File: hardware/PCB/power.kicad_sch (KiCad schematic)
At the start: 34 parts, among them J1 Screw_Terminal_01x02, U1 TPS62933, U2 TPS56837Hx, U4 TPS56837Hx

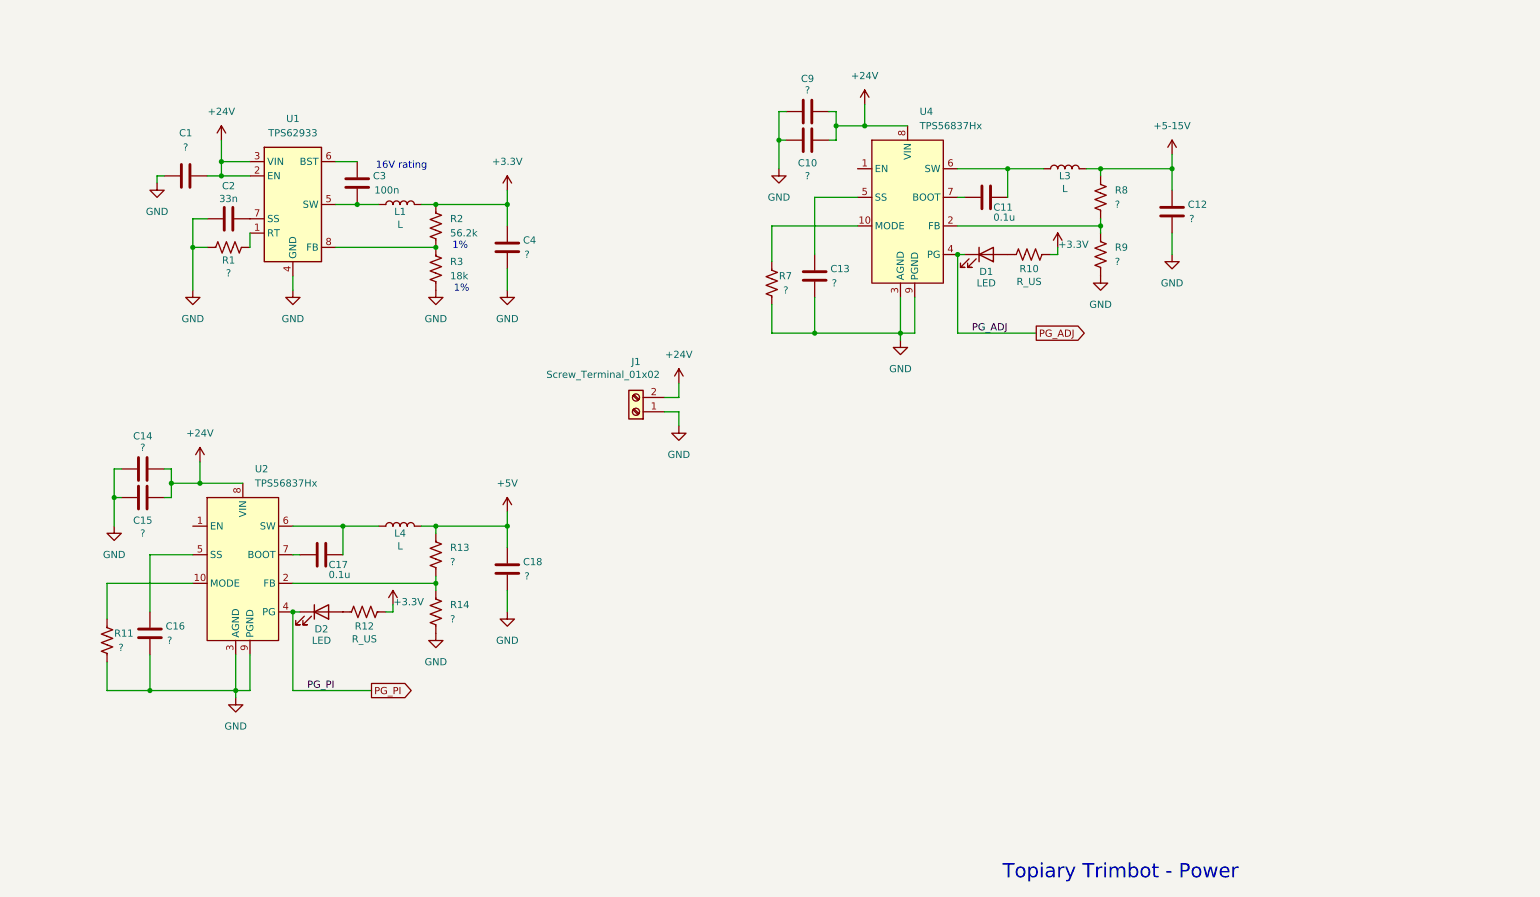
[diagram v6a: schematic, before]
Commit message: Schematic - Power Components
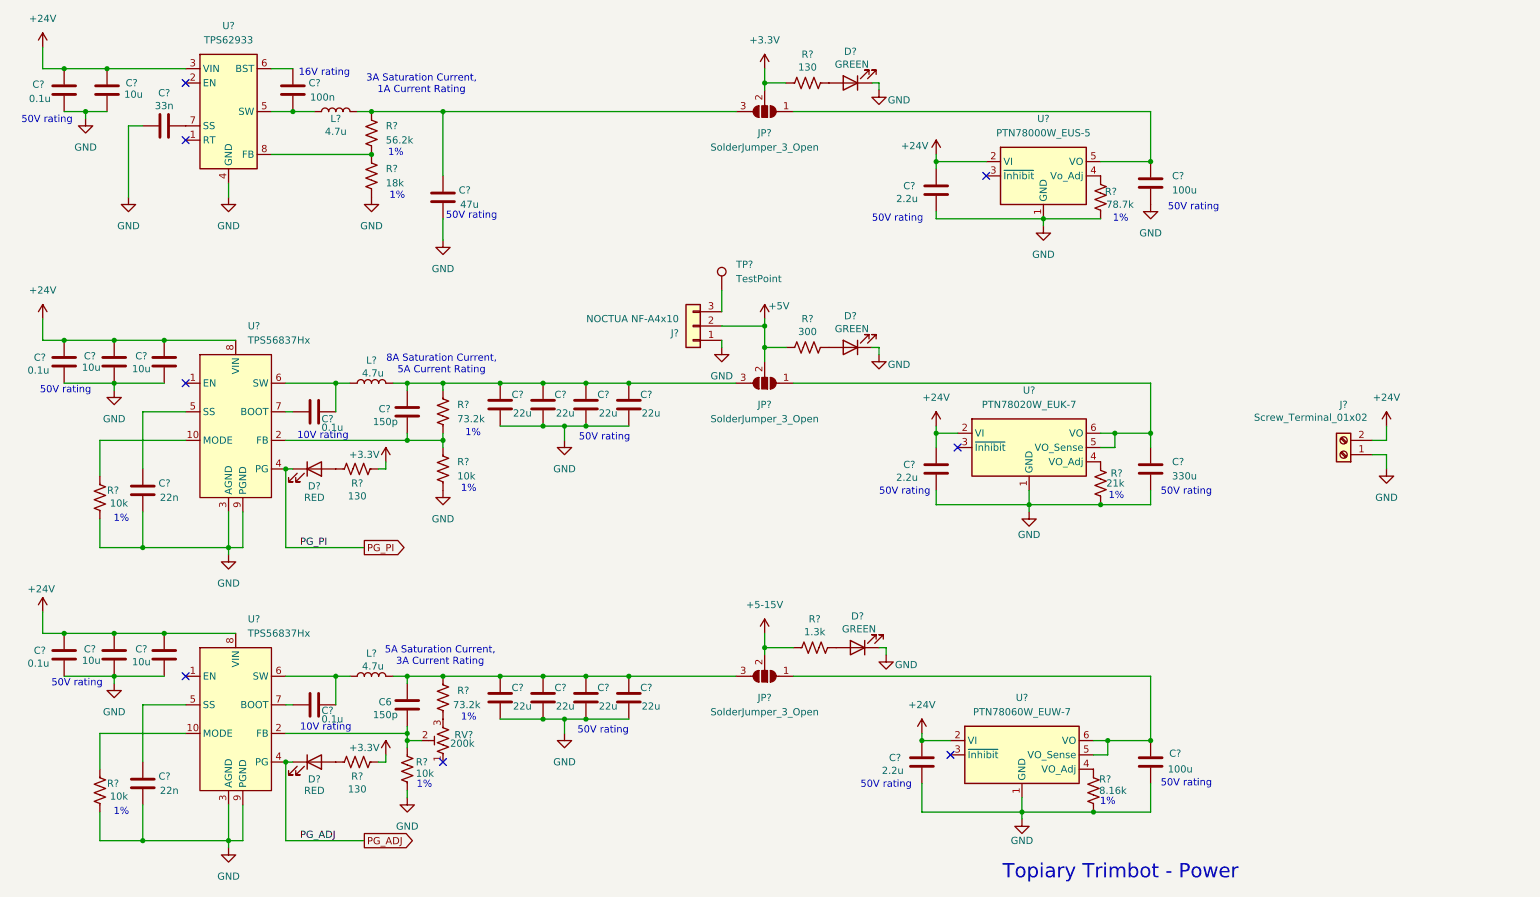
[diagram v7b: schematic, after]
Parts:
- removed C10, C12, C13, C9: ?, symbol Device:C
- removed C11: 0.1u, symbol Device:C
- removed D1: LED, symbol Device:LED
- removed L3: L, symbol Device:L
- removed R1, R7, R8, R9: ?, symbol Device:R_US
- removed R10: R_US, symbol Device:R_US
- removed U4: TPS56837Hx, CustomFootprints:RPA0010A-MFG, symbol CustomSymbols:TPS56837Hx
- added C6, C?: 150p, symbol Device:C
- added C? (x3): 10u, symbol Device:C
- added C?: 22n, symbol Device:C
- added C? (x7): 22u, symbol Device:C
- added C? (x3): 0.1u, symbol Device:C
- added C? (x3): 2.2u, symbol Device:C
- added C? (x2): 100u, symbol Device:C
- added C?: 330u, symbol Device:C
- added D? (x3): GREEN, symbol Device:LED
- added D?: RED, symbol Device:LED
- added J?: NOCTUA NF-A4x10, symbol Connector_Generic:Conn_01x03
- added JP? (x3): SolderJumper_3_Open, symbol Jumper:SolderJumper_3_Open
- added L?: 4.7u, symbol Device:L
- added R?: 300, symbol Device:R_US
- added R? (x2): 10k, symbol Device:R_US
- added R?: 1.3k, symbol Device:R_US
- added R? (x2): 130, symbol Device:R_US
- added R?: 21k, symbol Device:R_US
- added R?: 8.16k, symbol Device:R_US
- added R?: 73.2k, symbol Device:R_US
- added R?: 78.7k, symbol Device:R_US
- added RV?: 200k, symbol Device:R_Potentiometer_Trim_US
- added TP?: TestPoint, symbol Connector:TestPoint
- added U?: PTN78020W_EUK-7, Module:Texas_EUK_R-PDSS-T7_THT, symbol Converter_DCDC:PTN78020W_EUK-7
- added U?: PTN78000W_EUS-5, Module:Texas_EUS_R-PDSS-T5_THT, symbol Converter_DCDC:PTN78000W_EUS-5
- added U?: PTN78060W_EUW-7, Module:Texas_EUW_R-PDSS-T7_THT, symbol Converter_DCDC:PTN78060W_EUW-7
- added U?: TPS56837Hx, CustomFootprints:RPA0010A-MFG, symbol CustomSymbols:TPS56837Hx
- C?: renamed from C16; value ? -> 22n
- C?: renamed from C1; value ? -> 10u
- C?: renamed from C14; value ? -> 10u
- C?: renamed from C18; value ? -> 22u
- C?: renamed from C4; value ? -> 47u
- C?: renamed from C15; value ? -> 0.1u
- D?: renamed from D2; value LED -> RED
- L?: renamed from L1; value L -> 4.7u
- L?: renamed from L4; value L -> 4.7u
- R?: renamed from R12; value R_US -> 130
- R?: renamed from R11; value ? -> 10k
- R?: renamed from R14; value ? -> 10k
- R?: renamed from R13; value ? -> 73.2k
- renumbered C2 to C?, C17 to C?, C3 to C?, J1 to J?, R3 to R?, R2 to R?, U1 to U?, U2 to U?
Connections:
- net +24V: now also C?.1, C?.1, C?.1, C?.2, C?.2, C?.2, C?.2, C?.2, U?.2 (VI), U?.2 (VI), U?.2 (VI), U?.8 (VIN); no longer U?.2 (EN)
- net +3.3V: now also JP?.2 (C), R?.1, R?.2; no longer C?.1, L?.2, R?.1
- net +5-15V: now also JP?.2 (C), R?.2
- net +5V: now also J?.2 (Pin_2), JP?.2 (C), R?.2; no longer C?.1, L?.2, R?.1
- net GND: now also C?.1, C?.1, C?.1, C?.1, C?.1, C?.2, C?.2, C?.2, C?.2, C?.2, C?.2, C?.2, C?.2, C?.2, C?.2, C?.2, C?.2, C?.2, C?.2, D?.1 (K), D?.1 (K), D?.1 (K), J?.1 (Pin_1), R?.2, R?.2, R?.2, R?.2, R?.2, U?.1 (GND), U?.1 (GND), U?.1 (GND), U?.3 (AGND), U?.7 (GND), U?.7 (GND), U?.9 (PGND)
- net PG_ADJ: now also D?.1 (K), U?.4 (PG)
- net at R?.1, R?.2, U?.2 (FB): now also C?.2
- new net: C?.1, JP?.1 (A), U?.5 (VO_Sense), U?.6 (VO) (x2)
- new net: C6.1, C?.1, C?.1, C?.1, C?.1, JP?.3 (B), L?.2, R?.1
- new net: D?.2 (A), R?.1 (x3)
- new net: C?.1, U?.5 (SS)
- new net: C?.1, L?.1, U?.6 (SW)
- new net: C?.2, U?.7 (BOOT)
- new net: C?.1, C?.1, C?.1, C?.1, C?.1, JP?.3 (B), L?.2, R?.1
- new net: D?.2 (A), R?.2
- new net: R?.1, U?.4 (VO_Adj) (x2)
- new net: C?.1, JP?.1 (A), U?.5 (VO)
- new net: C?.1, JP?.3 (B), L?.2, R?.1
- new net: J?.3 (Pin_3), TP?.1
- new net: C6.2, R?.1, RV?.2, U?.2 (FB)
- new net: R?.2, RV?.3
- new net: R?.1, U?.4 (Vo_Adj)
- new net: R?.1, U?.10 (MODE)
- no-connect marks 0 -> 8
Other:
- note added: "10V rating"
- note added: "3A Saturation Current, 1A Current Rating"
- note added: "50V rating"
- note added: "5A Saturation Current, 3A Current Rating"
- note added: "8A Saturation Current, 5A Current Rating"
- moved on the sheet: C?, D?, J?, L?, R?, U?

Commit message: Schematic - Connector
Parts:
- removed J?: Screw_Terminal_01x02, symbol Connector:Screw_Terminal_01x02
- added J?: Screw_Terminal_01x04, symbol Connector:Screw_Terminal_01x04
- U?: MANUFACTURER (none) -> Texas Instruments; Manufacturer_Part_Number (none) -> TPS62933
- U? (x2): MANUFACTURER (none) -> Texas Instruments; Manufacturer_Part_Number (none) -> TPS56837Hx
- renumbered C6 to C?
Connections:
- net +24V: now also J?.1 (Pin_1), J?.2 (Pin_2)
- net GND: now also J?.3 (Pin_3), J?.4 (Pin_4)
